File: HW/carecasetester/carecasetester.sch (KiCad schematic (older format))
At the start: 11 parts, among them J4 Conn_01x06_Male, SW1 SW_DIP_x02

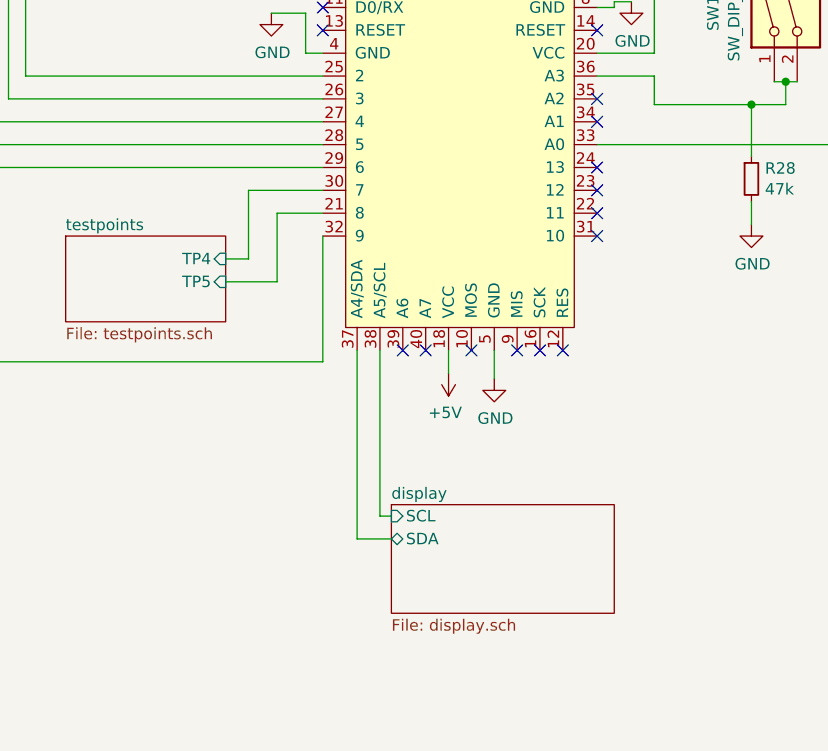
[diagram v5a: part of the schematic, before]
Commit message: CC tester : tp25 added tp8 moved tp20 moved
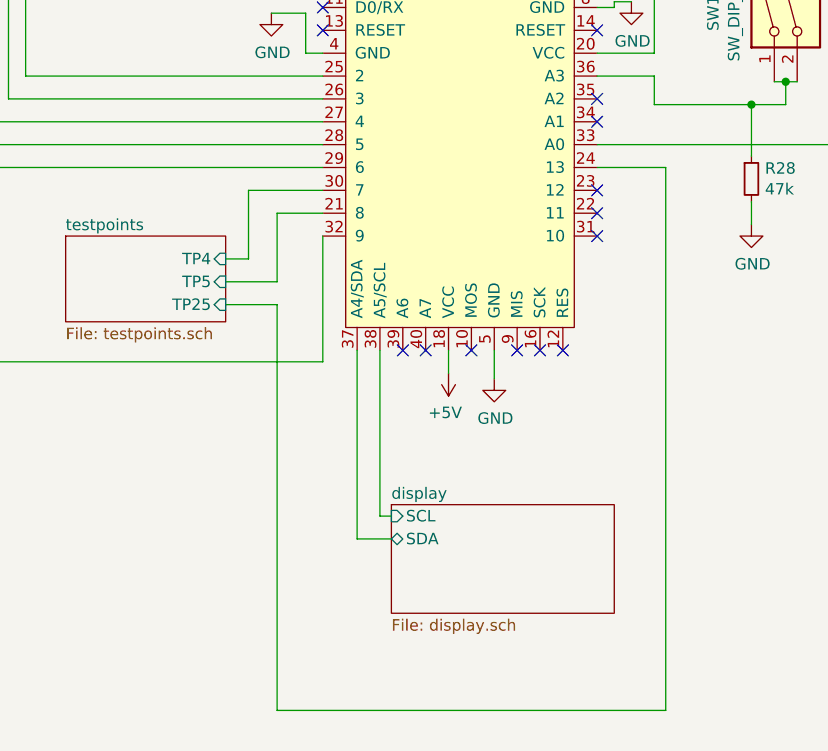
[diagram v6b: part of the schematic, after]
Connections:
- net testpoints/TP25: now reaches A1.24 (13)
- no-connect marks 17 -> 16
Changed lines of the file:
@@
 F2 "TP4" I R 4850 3900 50
 F3 "TP5" I R 4850 4000 50
+F4 "TP25" I R 4850 4100 50
 $EndSheet
 Wire Wire Line
@@
 NoConn ~ 6225 4300
 NoConn ~ 6325 4300
-NoConn ~ 6475 3800
 NoConn ~ 6475 3700
 NoConn ~ 6475 3600
-NoConn ~ 6475 3500
+NoConn ~ 6475 3800
 NoConn ~ 6475 3300
 NoConn ~ 6475 3200
@@
 Wire Wire Line
 	3750 3950 3400 3950
+Wire Wire Line
+	4850 4100 5075 4100
+Wire Wire Line
+	5075 4100 5075 5875
+Wire Wire Line
+	5075 5875 6775 5875
+Wire Wire Line
+	6775 3500 6475 3500
+Wire Wire Line
+	6775 3500 6775 5875
 $EndSCHEMATC
